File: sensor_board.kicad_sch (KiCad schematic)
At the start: 49 parts, among them U1 AMS1117-3.3, U2 STM32H753IITx

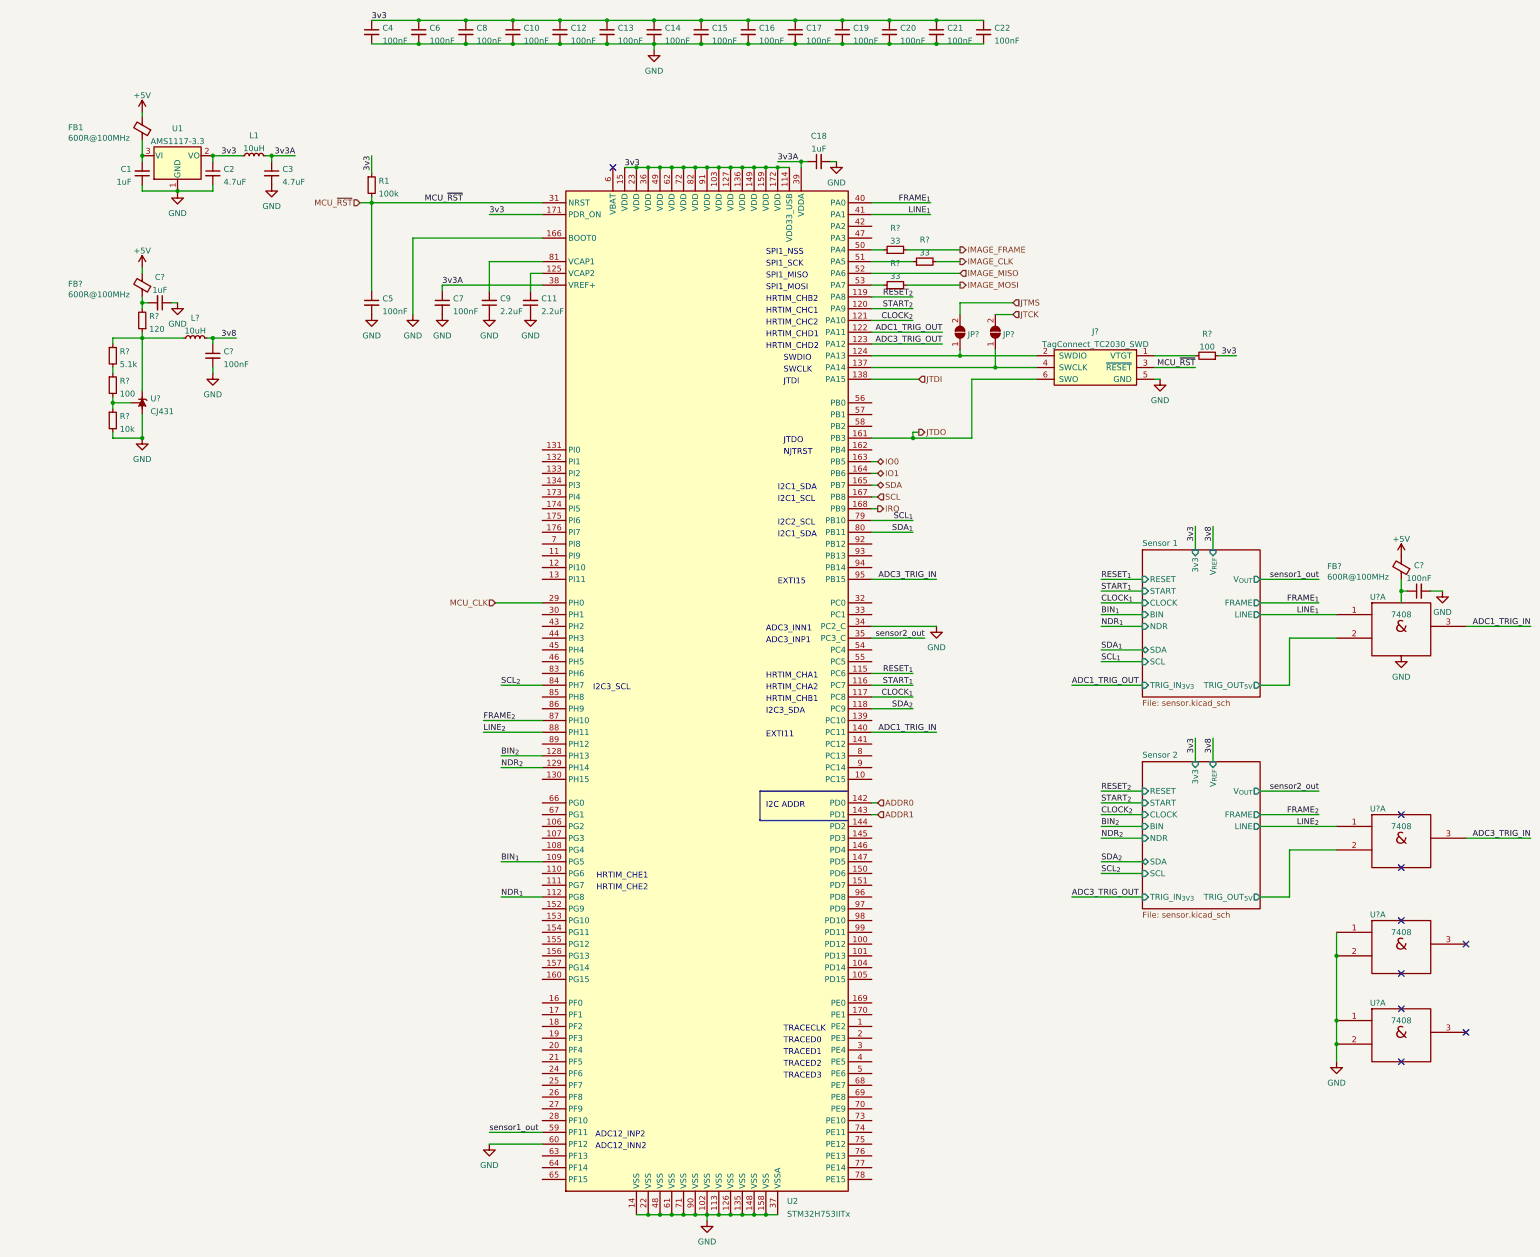
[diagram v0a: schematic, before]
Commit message: Add RadEye1 sensor reference voltage supply
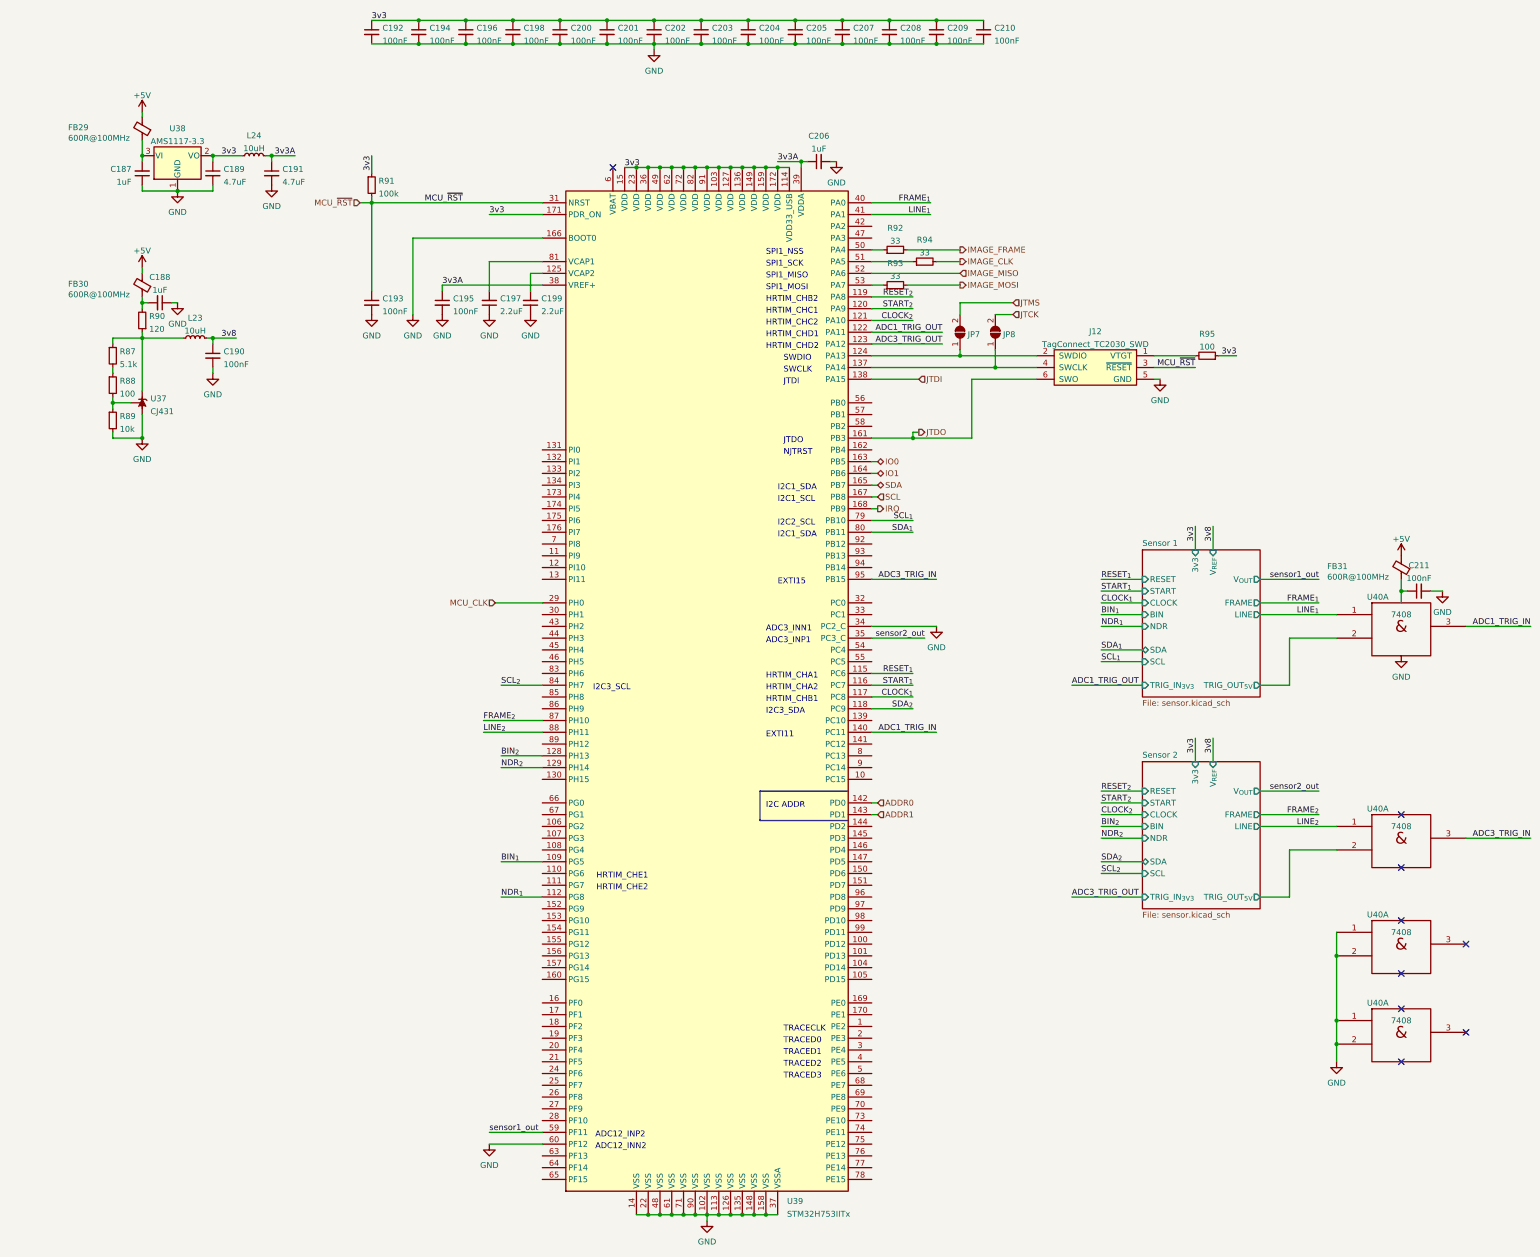
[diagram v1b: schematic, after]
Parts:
- gave numbers to parts that had none: 19
- renumbered C1 to C187, C2 to C189, C3 to C191, C4 to C192, C5 to C193, C6 to C194, C7 to C195, C8 to C196, C9 to C197, C10 to C198, C11 to C199, C12 to C200, C13 to C201, C14 to C202, C15 to C203, C16 to C204, C17 to C205, C18 to C206, C19 to C207, C20 to C208, C21 to C209, C22 to C210, FB1 to FB29, L1 to L24, R1 to R91, U1 to U38, U2 to U39
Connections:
- net GND: now also C187.1, C189.2, U38.1 (GND)

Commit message: Fix shifted FMC D30 and D31 on main STM32
Pins for D30 and D31 were shifted up by one pin
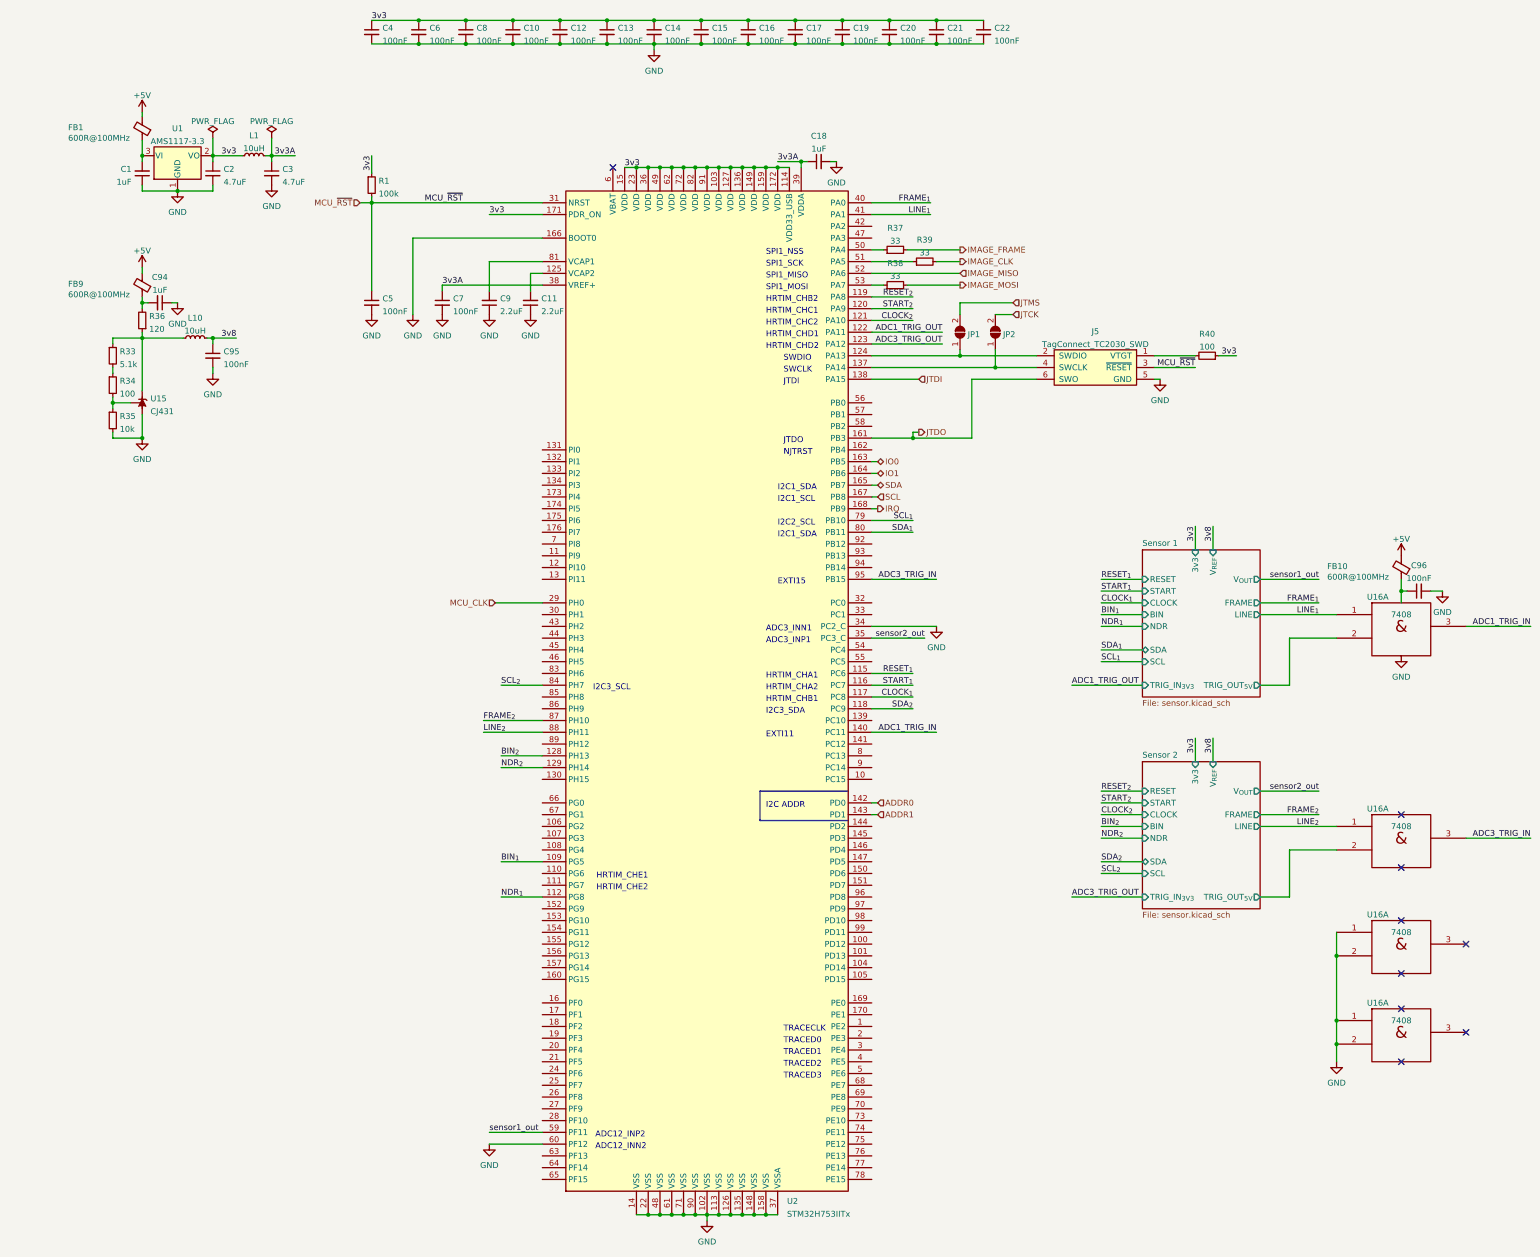
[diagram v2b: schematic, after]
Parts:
- renumbered C187 to C1, C198 to C10, C199 to C11, C200 to C12, C201 to C13, C202 to C14, C203 to C15, C204 to C16, C205 to C17, C206 to C18, C207 to C19, C189 to C2, C208 to C20, C209 to C21, C210 to C22, C191 to C3, C192 to C4, C193 to C5, C194 to C6, C195 to C7, C196 to C8, C197 to C9, C188 to C94, C190 to C95, C211 to C96, FB29 to FB1, FB31 to FB10, FB30 to FB9, J12 to J5, JP7 to JP1, JP8 to JP2, L24 to L1, L23 to L10, R91 to R1, R87 to R33, R88 to R34, R89 to R35, R90 to R36, R92 to R37, R93 to R38, R94 to R39, R95 to R40, U38 to U1, U37 to U15, U40 to U16, U39 to U2

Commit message: Use FC1-15-02-T-WT connector for RadEye1 modules
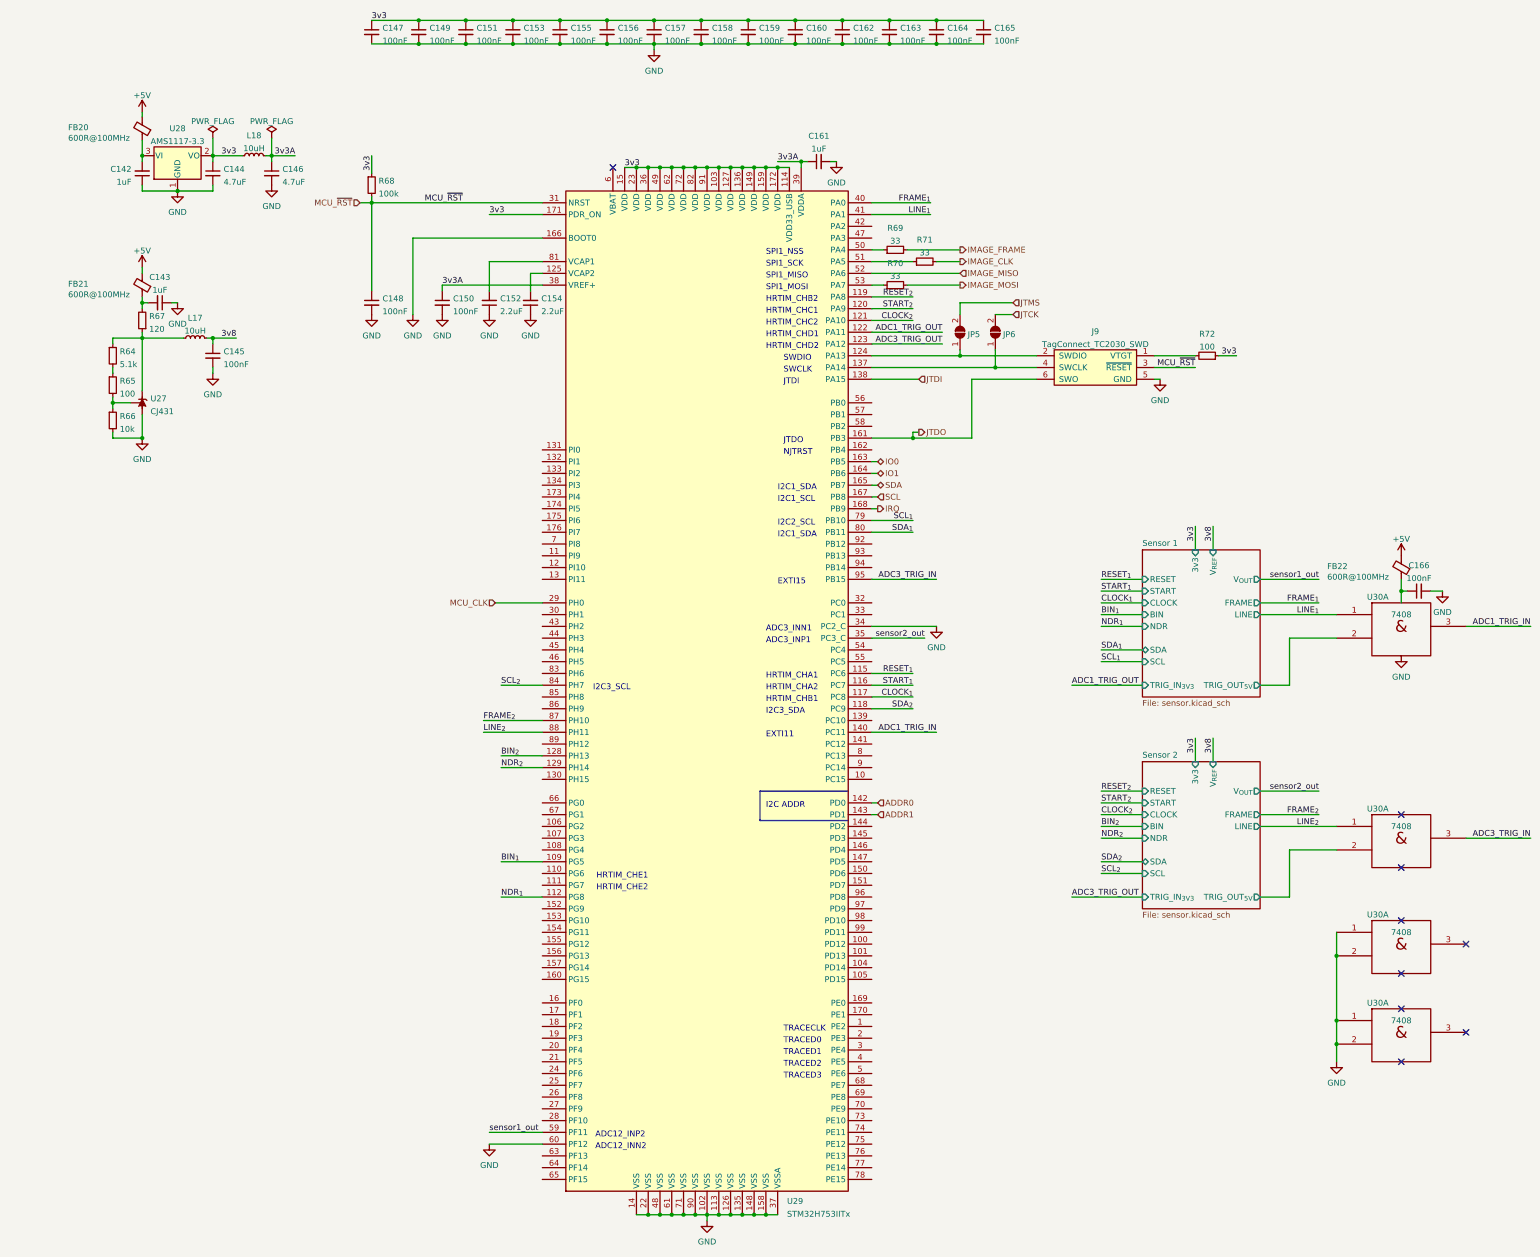
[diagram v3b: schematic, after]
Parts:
- renumbered C1 to C142, C94 to C143, C2 to C144, C95 to C145, C3 to C146, C4 to C147, C5 to C148, C6 to C149, C7 to C150, C8 to C151, C9 to C152, C10 to C153, C11 to C154, C12 to C155, C13 to C156, C14 to C157, C15 to C158, C16 to C159, C17 to C160, C18 to C161, C19 to C162, C20 to C163, C21 to C164, C22 to C165, C96 to C166, FB1 to FB20, FB9 to FB21, FB10 to FB22, J5 to J9, JP1 to JP5, JP2 to JP6, L10 to L17, L1 to L18, R33 to R64, R34 to R65, R35 to R66, R36 to R67, R1 to R68, R37 to R69, R38 to R70, R39 to R71, R40 to R72, U15 to U27, U1 to U28, U2 to U29, U16 to U30

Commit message: First acquisition channel layout WiP
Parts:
- added C?: 100nF, Capacitor_SMD:C_0402_1005Metric, symbol Device:C_Small
- renumbered C142 to C1, C153 to C10, C154 to C11, C155 to C12, C156 to C13, C157 to C14, C158 to C15, C159 to C16, C160 to C17, C161 to C18, C162 to C19, C144 to C2, C163 to C20, C164 to C21, C165 to C22, C146 to C3, C147 to C4, C148 to C5, C149 to C6, C150 to C7, C151 to C8, C152 to C9, C143 to C94, C145 to C95, C166 to C96, FB20 to FB1, FB22 to FB10, FB21 to FB9, J9 to J5, JP5 to JP1, JP6 to JP2, L18 to L1, L17 to L10, R68 to R1, R64 to R33, R65 to R34, R66 to R35, R67 to R36, R69 to R37, R70 to R38, R71 to R39, R72 to R40, U28 to U1, U27 to U15, U30 to U16, U29 to U2
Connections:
- net 3v3: now also C?.1
- net GND: now also C?.2
